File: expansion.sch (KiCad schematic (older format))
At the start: 3 parts, among them J7 DF40HC(3.5)-60DS, J9 DF40HC(3.5)-60DS, U1 IMX8MM

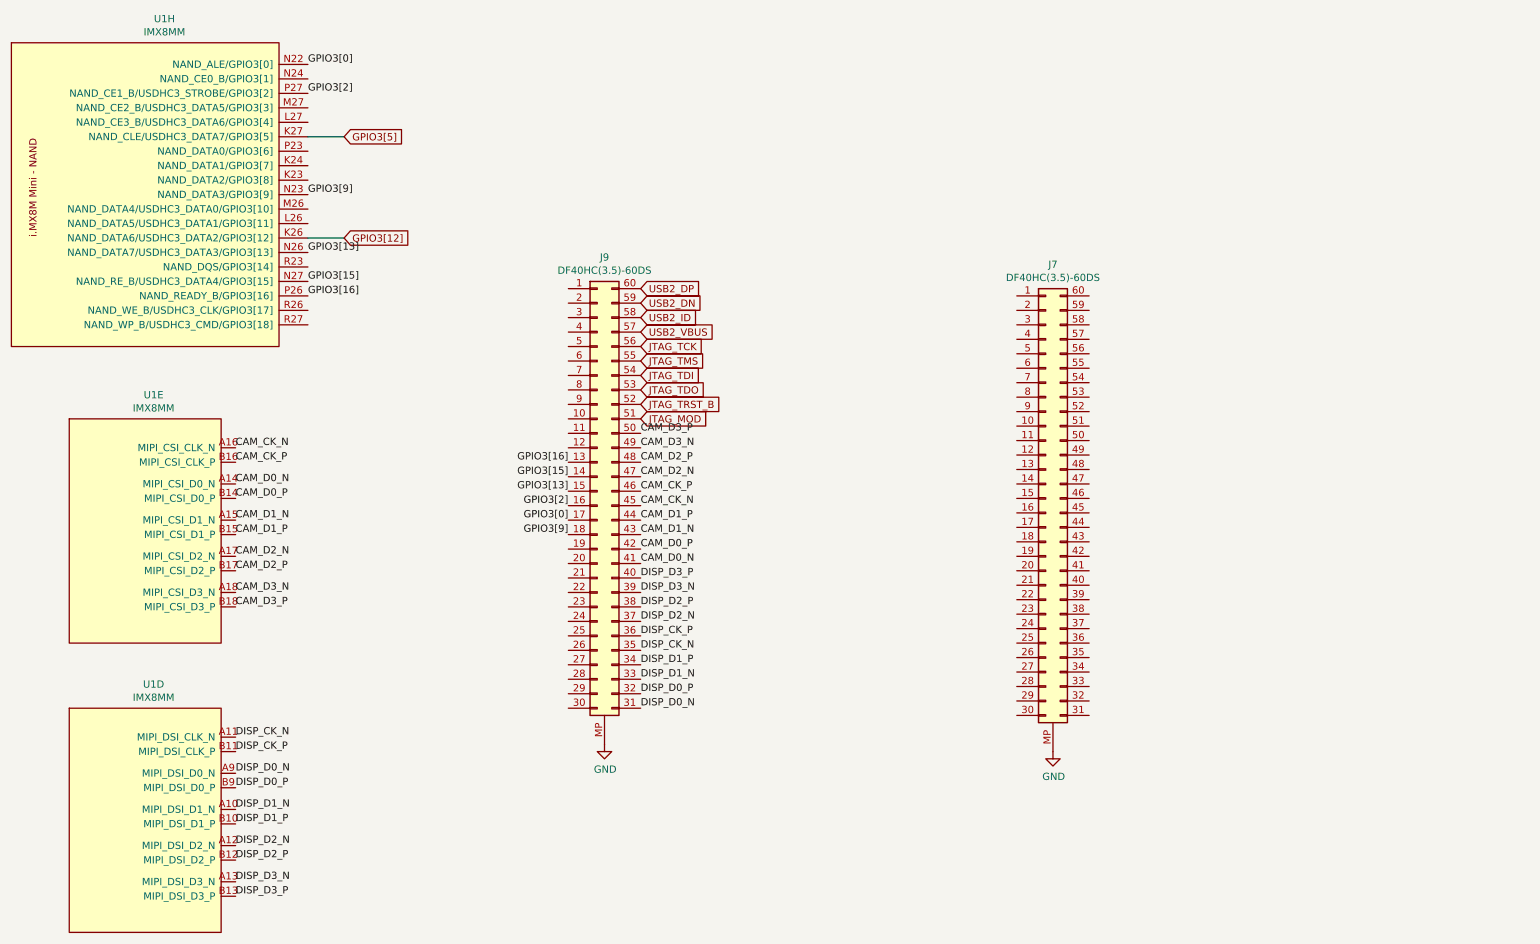
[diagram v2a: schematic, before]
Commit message: add sai, mdio, sdhc to headers
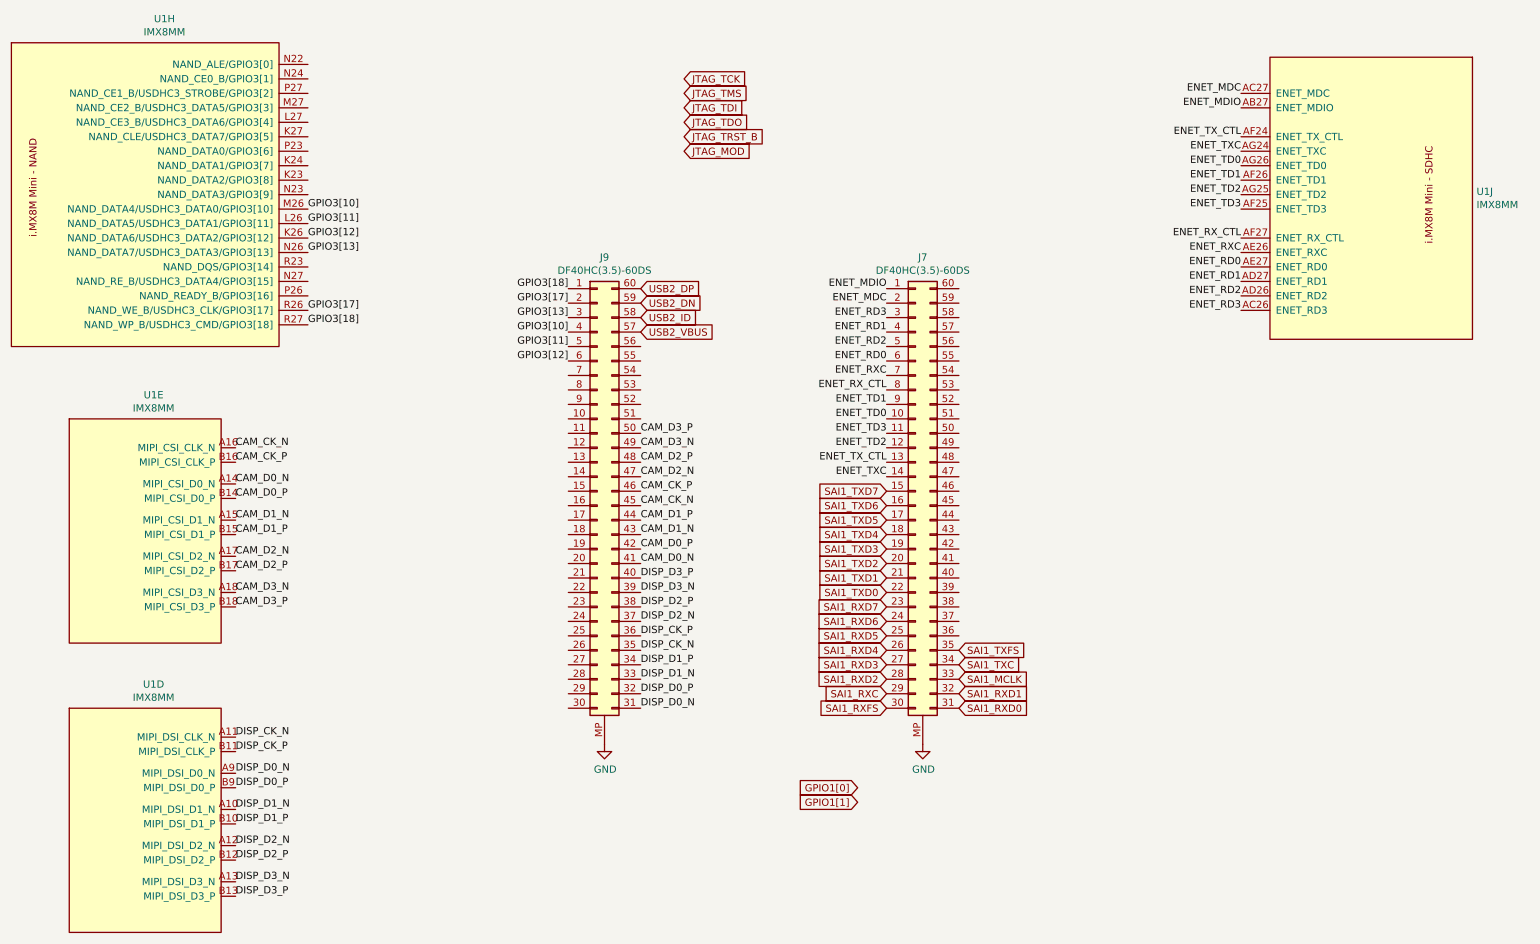
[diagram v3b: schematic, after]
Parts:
- added unit 10 of U1
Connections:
- net GPIO3[12]: now also J9.6 (Pin_6)
- net GPIO3[13]: now also J9.3 (Pin_3); no longer J9.15 (Pin_15)
- net JTAG_MOD: no longer J9.51 (Pin_51)
- net JTAG_TCK: no longer J9.56 (Pin_56)
- net JTAG_TDI: no longer J9.54 (Pin_54)
- net JTAG_TDO: no longer J9.53 (Pin_53)
- net JTAG_TMS: no longer J9.55 (Pin_55)
- net JTAG_TRST_B: no longer J9.52 (Pin_52)
- net GPIO3[18]: now reaches J9.1 (Pin_1)
- net GPIO3[18]: now also U1.R27 (NAND_WP_B/USDHC3_CMD/GPIO3[18])
- net GPIO3[17]: now reaches J9.2 (Pin_2)
- net GPIO3[17]: now also U1.R26 (NAND_WE_B/USDHC3_CLK/GPIO3[17])
- net GPIO3[10]: now reaches J9.4 (Pin_4)
- net GPIO3[10]: now also U1.M26 (NAND_DATA4/USDHC3_DATA0/GPIO3[10])
- net GPIO3[11]: now reaches J9.5 (Pin_5)
- net GPIO3[11]: now also U1.L26 (NAND_DATA5/USDHC3_DATA1/GPIO3[11])
- net ENET_MDIO: now reaches J7.1 (Pin_1)
- net ENET_MDIO: now also U1.AB27 (ENET_MDIO)
- net ENET_TD0: now reaches J7.10 (Pin_10)
- net ENET_TD0: now also U1.AG26 (ENET_TD0)
- net ENET_TD3: now reaches J7.11 (Pin_11)
- net ENET_TD3: now also U1.AF25 (ENET_TD3)
- net ENET_TD2: now reaches J7.12 (Pin_12)
- net ENET_TD2: now also U1.AG25 (ENET_TD2)
- net ENET_TX_CTL: now reaches J7.13 (Pin_13)
- net ENET_TX_CTL: now also U1.AF24 (ENET_TX_CTL)
- net ENET_TXC: now reaches J7.14 (Pin_14)
- net ENET_TXC: now also U1.AG24 (ENET_TXC)
- net SAI1_TXD7: now reaches J7.15 (Pin_15)
- net SAI1_TXD6: now reaches J7.16 (Pin_16)
- net SAI1_TXD5: now reaches J7.17 (Pin_17)
- net SAI1_TXD4: now reaches J7.18 (Pin_18)
- net SAI1_TXD3: now reaches J7.19 (Pin_19)
- net ENET_MDC: now reaches J7.2 (Pin_2)
- net ENET_MDC: now also U1.AC27 (ENET_MDC)
- net SAI1_TXD2: now reaches J7.20 (Pin_20)
- net SAI1_TXD1: now reaches J7.21 (Pin_21)
- net SAI1_TXD0: now reaches J7.22 (Pin_22)
- net SAI1_RXD7: now reaches J7.23 (Pin_23)
- net SAI1_RXD6: now reaches J7.24 (Pin_24)
- net SAI1_RXD5: now reaches J7.25 (Pin_25)
- net SAI1_RXD4: now reaches J7.26 (Pin_26)
- net SAI1_RXD3: now reaches J7.27 (Pin_27)
- net SAI1_RXD2: now reaches J7.28 (Pin_28)
- net SAI1_RXC: now reaches J7.29 (Pin_29)
- net ENET_RD3: now reaches J7.3 (Pin_3)
- net ENET_RD3: now also U1.AC26 (ENET_RD3)
- net SAI1_RXFS: now reaches J7.30 (Pin_30)
- net SAI1_RXD0: now reaches J7.31 (Pin_31)
- net SAI1_RXD1: now reaches J7.32 (Pin_32)
- net SAI1_MCLK: now reaches J7.33 (Pin_33)
- net SAI1_TXC: now reaches J7.34 (Pin_34)
- net SAI1_TXFS: now reaches J7.35 (Pin_35)
- net ENET_RD1: now reaches J7.4 (Pin_4)
- net ENET_RD1: now also U1.AD27 (ENET_RD1)
- net ENET_RD2: now reaches J7.5 (Pin_5)
- net ENET_RD2: now also U1.AD26 (ENET_RD2)
- net ENET_RD0: now reaches J7.6 (Pin_6)
- net ENET_RD0: now also U1.AE27 (ENET_RD0)
- net ENET_RXC: now reaches J7.7 (Pin_7)
- net ENET_RXC: now also U1.AE26 (ENET_RXC)
- net ENET_RX_CTL: now reaches J7.8 (Pin_8)
- net ENET_RX_CTL: now also U1.AF27 (ENET_RX_CTL)
- net ENET_TD1: now reaches J7.9 (Pin_9)
- net ENET_TD1: now also U1.AF26 (ENET_TD1)
- net GPIO3[0]: no longer names the net of J9.17 (Pin_17)
- net GPIO3[0]: no longer U1.N22 (NAND_ALE/GPIO3[0])
- net GPIO3[15]: no longer names the net of J9.14 (Pin_14)
- net GPIO3[15]: no longer U1.N27 (NAND_RE_B/USDHC3_DATA4/GPIO3[15])
- net GPIO3[16]: no longer names the net of J9.13 (Pin_13)
- net GPIO3[16]: no longer U1.P26 (NAND_READY_B/GPIO3[16])
- net GPIO3[2]: no longer names the net of J9.16 (Pin_16)
- net GPIO3[2]: no longer U1.P27 (NAND_CE1_B/USDHC3_STROBE/GPIO3[2])
- net GPIO3[5]: no longer names the net of U1.K27 (NAND_CLE/USDHC3_DATA7/GPIO3[5])
- net GPIO3[9]: no longer names the net of J9.18 (Pin_18)
- net GPIO3[9]: no longer U1.N23 (NAND_DATA3/GPIO3[9])
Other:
- moved on the sheet: J7
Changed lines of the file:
@@
 L Connector_Generic:Conn_02x30_Counter_Clockwise J?
 U 1 1 5E36744C
-P 7850 4000
+P 6950 3950
 AR Path="/5E36744C" Ref="J?"  Part="1"
 AR Path="/5E34BAA5/5E36744C" Ref="J7"  Part="1"
-F 0 "J7" H 7900 5617 50  0000 C CNN
-F 1 "DF40HC(3.5)-60DS" H 7900 5526 50  0000 C CNN
-F 2 "mxenc:DF40C-60DP" H 7850 4000 50  0001 C CNN
-F 3 "~" H 7850 4000 50  0001 C CNN
-	1    7850 4000
+F 0 "J7" H 7000 5567 50  0000 C CNN
+F 1 "DF40HC(3.5)-60DS" H 7000 5476 50  0000 C CNN
+F 2 "mxenc:DF40C-60DP" H 6950 3950 50  0001 C CNN
+F 3 "~" H 6950 3950 50  0001 C CNN
+	1    6950 3950
 	1    0    0    -1
 $EndComp
@@
 L power:GND #PWR0152
 U 1 1 5E62D325
-P 7900 5750
-F 0 "#PWR0152" H 7900 5500 50  0001 C CNN
-F 1 "GND" H 7905 5577 50  0000 C CNN
-F 2 "" H 7900 5750 50  0001 C CNN
-F 3 "" H 7900 5750 50  0001 C CNN
-	1    7900 5750
-	1    0    0    -1
-$EndComp
-Text GLabel 5050 2950 2    50   Input ~ 0
+P 7000 5700
+F 0 "#PWR0152" H 7000 5450 50  0001 C CNN
+F 1 "GND" H 7005 5527 50  0000 C CNN
+F 2 "" H 7000 5700 50  0001 C CNN
+F 3 "" H 7000 5700 50  0001 C CNN
+	1    7000 5700
+	1    0    0    -1
+$EndComp
+Text GLabel 5350 1100 2    50   Input ~ 0
 JTAG_TCK
-Text GLabel 5050 3050 2    50   Input ~ 0
+Text GLabel 5350 1200 2    50   Input ~ 0
 JTAG_TMS
-Text GLabel 5050 3150 2    50   Input ~ 0
+Text GLabel 5350 1300 2    50   Input ~ 0
 JTAG_TDI
-Text GLabel 5050 3250 2    50   Input ~ 0
+Text GLabel 5350 1400 2    50   Input ~ 0
 JTAG_TDO
-Text GLabel 5050 3350 2    50   Input ~ 0
+Text GLabel 5350 1500 2    50   Input ~ 0
 JTAG_TRST_B
-Text GLabel 5050 3450 2    50   Input ~ 0
+Text GLabel 5350 1600 2    50   Input ~ 0
 JTAG_MOD
 $Comp
@@
 	1    0    0    -1
 $EndComp
-Text GLabel 3000 2200 2    50   Input ~ 0
-GPIO3[12]
-Wire Wire Line
-	3000 2200 2750 2200
-Wire Wire Line
-	3000 1500 2750 1500
-Text GLabel 3000 1500 2    50   Input ~ 0
-GPIO3[5]
 Text Label 2750 2300 0    50   ~ 0
 GPIO3[13]
-Text Label 2750 2500 0    50   ~ 0
-GPIO3[15]
-Text Label 2750 2600 0    50   ~ 0
-GPIO3[16]
-Text Label 2750 1200 0    50   ~ 0
-GPIO3[2]
-Text Label 2750 1000 0    50   ~ 0
-GPIO3[0]
-Text Label 2750 1900 0    50   ~ 0
-GPIO3[9]
-Text Label 4550 4150 2    50   ~ 0
-GPIO3[0]
-Text Label 4550 4250 2    50   ~ 0
-GPIO3[9]
-Text Label 4550 3950 2    50   ~ 0
+Text Label 2750 2700 0    50   ~ 0
+GPIO3[17]
+Text GLabel 6550 6000 0    50   Input ~ 0
+GPIO1[0]
+Text GLabel 6550 6100 0    50   Input ~ 0
+GPIO1[1]
+$Comp
+L mxenc:MIMX8MM6DVTLZAA U1
+U 10 1 5EACF487
+P 10100 3650
+F 0 "U1" H 9372 5421 50  0000 R CNN
+F 1 "IMX8MM" H 9372 5330 50  0000 R CNN
+F 2 "mxenc:BGA-729_27x27_14.0x14.0mm" H 10350 6400 50  0001 C CNN
+F 3 "" H 9300 6400 50  0001 C CNN
+	10   10100 3650
+	-1   0    0    -1
+$EndComp
+Text Label 9200 1200 2    50   ~ 0
+ENET_MDC
+Text Label 9200 1300 2    50   ~ 0
+ENET_MDIO
+Text Label 9200 1500 2    50   ~ 0
+ENET_TX_CTL
+Text Label 9200 1600 2    50   ~ 0
+ENET_TXC
+Text Label 9200 1700 2    50   ~ 0
+ENET_TD0
+Text Label 9200 1800 2    50   ~ 0
+ENET_TD1
+Text Label 9200 1900 2    50   ~ 0
+ENET_TD2
+Text Label 9200 2000 2    50   ~ 0
+ENET_TD3
+Text Label 9200 2200 2    50   ~ 0
+ENET_RX_CTL
+Text Label 9200 2300 2    50   ~ 0
+ENET_RXC
+Text Label 9200 2400 2    50   ~ 0
+ENET_RD0
+Text Label 9200 2500 2    50   ~ 0
+ENET_RD1
+Text Label 9200 2600 2    50   ~ 0
+ENET_RD2
+Text Label 9200 2700 2    50   ~ 0
+ENET_RD3
+Text Label 6750 2650 2    50   ~ 0
+ENET_MDC
+Text Label 6750 2550 2    50   ~ 0
+ENET_MDIO
+Text Label 6750 3750 2    50   ~ 0
+ENET_TX_CTL
+Text Label 6750 3850 2    50   ~ 0
+ENET_TXC
+Text Label 6750 3450 2    50   ~ 0
+ENET_TD0
+Text Label 6750 3350 2    50   ~ 0
+ENET_TD1
+Text Label 6750 3650 2    50   ~ 0
+ENET_TD2
+Text Label 6750 3550 2    50   ~ 0
+ENET_TD3
+Text Label 6750 3250 2    50   ~ 0
+ENET_RX_CTL
+Text Label 6750 3150 2    50   ~ 0
+ENET_RXC
+Text Label 6750 3050 2    50   ~ 0
+ENET_RD0
+Text Label 6750 2850 2    50   ~ 0
+ENET_RD1
+Text Label 6750 2950 2    50   ~ 0
+ENET_RD2
+Text Label 6750 2750 2    50   ~ 0
+ENET_RD3
+Text GLabel 6750 3950 0    50   Input ~ 0
+SAI1_TXD7
+Text GLabel 6750 4050 0    50   Input ~ 0
+SAI1_TXD6
+Text GLabel 6750 4150 0    50   Input ~ 0
+SAI1_TXD5
+Text GLabel 6750 4250 0    50   Input ~ 0
+SAI1_TXD4
+Text GLabel 6750 4350 0    50   Input ~ 0
+SAI1_TXD3
+Text GLabel 6750 4450 0    50   Input ~ 0
+SAI1_TXD2
+Text GLabel 6750 4550 0    50   Input ~ 0
+SAI1_TXD1
+Text GLabel 6750 4650 0    50   Input ~ 0
+SAI1_TXD0
+Text GLabel 6750 4750 0    50   Input ~ 0
+SAI1_RXD7
+Text GLabel 6750 4850 0    50   Input ~ 0
+SAI1_RXD6
+Text GLabel 6750 4950 0    50   Input ~ 0
+SAI1_RXD5
+Text GLabel 6750 5050 0    50   Input ~ 0
+SAI1_RXD4
+Text GLabel 6750 5150 0    50   Input ~ 0
+SAI1_RXD3
+Text GLabel 6750 5250 0    50   Input ~ 0
+SAI1_RXD2
+Text GLabel 6750 5350 0    50   Input ~ 0
+SAI1_RXC
+Text GLabel 6750 5450 0    50   Input ~ 0
+SAI1_RXFS
+Text GLabel 7250 5350 2    50   Input ~ 0
+SAI1_RXD1
+Text GLabel 7250 5450 2    50   Input ~ 0
+SAI1_RXD0
+Text GLabel 7250 5150 2    50   Input ~ 0
+SAI1_TXC
+Text GLabel 7250 5050 2    50   Input ~ 0
+SAI1_TXFS
+Text GLabel 7250 5250 2    50   Input ~ 0
+SAI1_MCLK
+Text Label 2750 2800 0    50   ~ 0
+GPIO3[18]
+Text Label 2750 2200 0    50   ~ 0
+GPIO3[12]
+Text Label 2750 2100 0    50   ~ 0
+GPIO3[11]
+Text Label 2750 2000 0    50   ~ 0
+GPIO3[10]
+Text Label 4550 3050 2    50   ~ 0
+GPIO3[12]
+Text Label 4550 2550 2    50   ~ 0
+GPIO3[18]
+Text Label 4550 2650 2    50   ~ 0
+GPIO3[17]
+Text Label 4550 2750 2    50   ~ 0
 GPIO3[13]
-Text Label 4550 3850 2    50   ~ 0
-GPIO3[15]
-Text Label 4550 3750 2    50   ~ 0
-GPIO3[16]
-Text Label 4550 4050 2    50   ~ 0
-GPIO3[2]
+Text Label 4550 2850 2    50   ~ 0
+GPIO3[10]
+Text Label 4550 2950 2    50   ~ 0
+GPIO3[11]
 $EndSCHEMATC

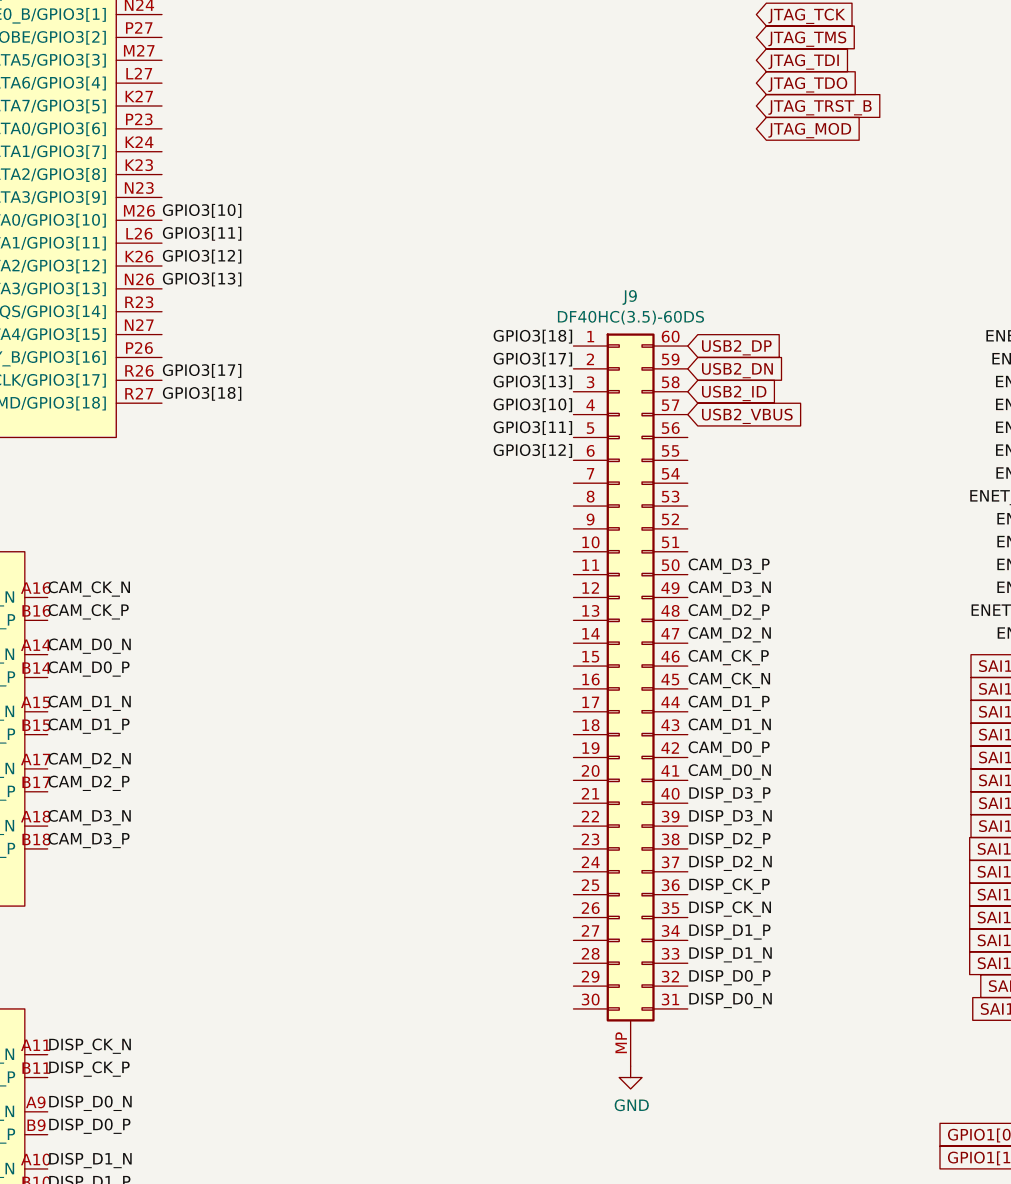
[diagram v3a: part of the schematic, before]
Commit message: Ground mounting pads and route ecspi to expansion
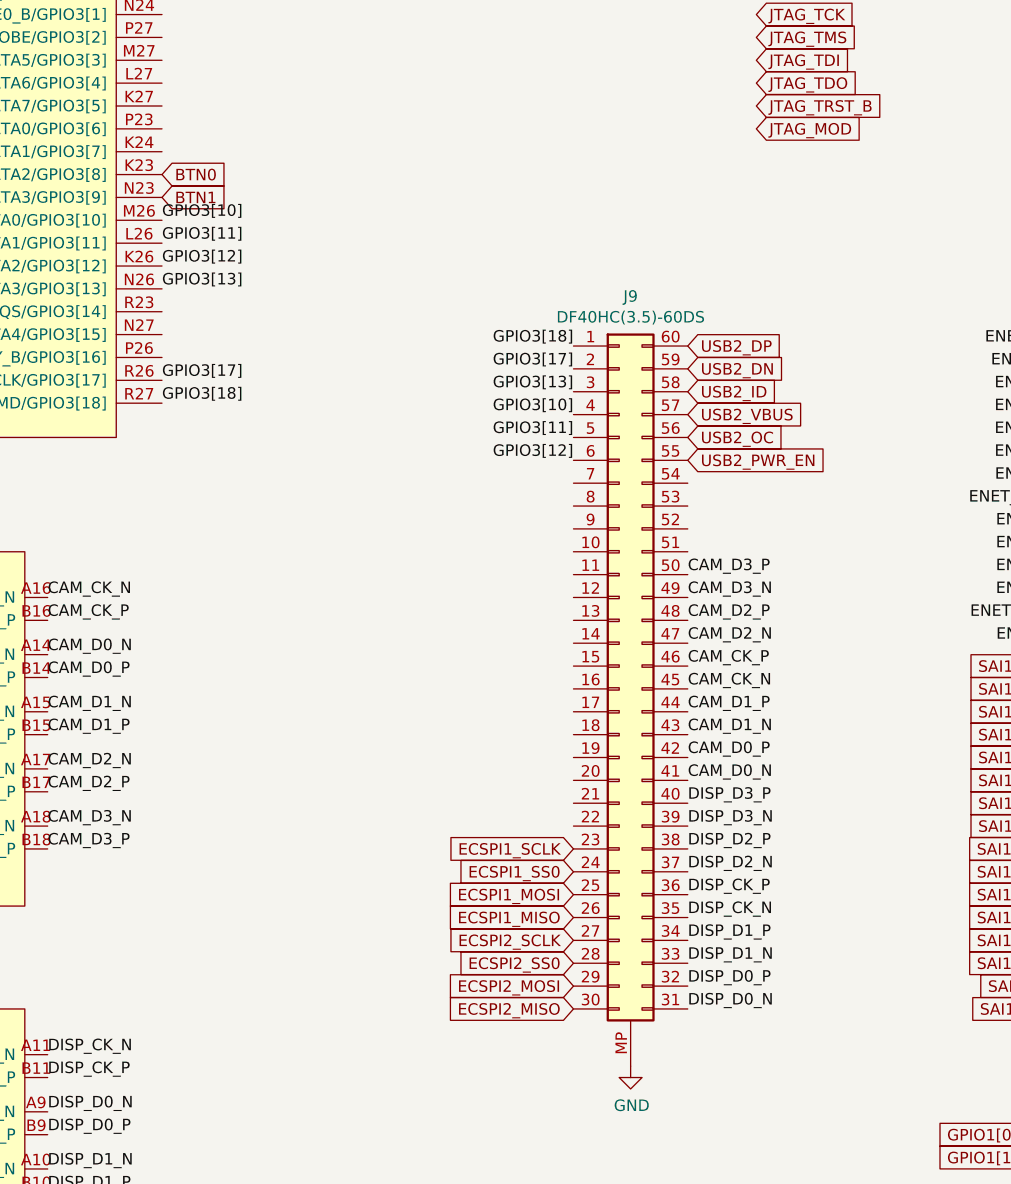
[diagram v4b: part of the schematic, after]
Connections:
- net ECSPI1_SCLK: now reaches J9.23 (Pin_23)
- net ECSPI1_SS0: now reaches J9.24 (Pin_24)
- net ECSPI1_MOSI: now reaches J9.25 (Pin_25)
- net ECSPI1_MISO: now reaches J9.26 (Pin_26)
- net ECSPI2_SCLK: now reaches J9.27 (Pin_27)
- net ECSPI2_SS0: now reaches J9.28 (Pin_28)
- net ECSPI2_MOSI: now reaches J9.29 (Pin_29)
- net ECSPI2_MISO: now reaches J9.30 (Pin_30)
- net USB2_PWR_EN: now reaches J9.55 (Pin_55)
- net USB2_OC: now reaches J9.56 (Pin_56)
- net BTN0: now reaches U1.K23 (NAND_DATA2/GPIO3[8])
- net BTN1: now reaches U1.N23 (NAND_DATA3/GPIO3[9])
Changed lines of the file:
@@
 Text Label 4550 2950 2    50   ~ 0
 GPIO3[11]
+Text GLabel 2750 1800 2    50   Input ~ 0
+BTN0
+Text GLabel 2750 1900 2    50   Input ~ 0
+BTN1
+Text GLabel 5050 2950 2    50   Input ~ 0
+USB2_OC
+Text GLabel 5050 3050 2    50   Input ~ 0
+USB2_PWR_EN
+Text GLabel 4550 5150 0    50   Input ~ 0
+ECSPI2_SCLK
+Text GLabel 4550 5450 0    50   Input ~ 0
+ECSPI2_MISO
+Text GLabel 4550 5350 0    50   Input ~ 0
+ECSPI2_MOSI
+Text GLabel 4550 5250 0    50   Input ~ 0
+ECSPI2_SS0
+Text GLabel 4550 4750 0    50   Input ~ 0
+ECSPI1_SCLK
+Text GLabel 4550 5050 0    50   Input ~ 0
+ECSPI1_MISO
+Text GLabel 4550 4950 0    50   Input ~ 0
+ECSPI1_MOSI
+Text GLabel 4550 4850 0    50   Input ~ 0
+ECSPI1_SS0
 $EndSCHEMATC
